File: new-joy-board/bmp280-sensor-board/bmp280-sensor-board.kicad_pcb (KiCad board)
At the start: 2 copper layers, 26.1 x 31.1 mm, 16 parts, among them J1 Conn_01x05, U1 TPS76933, U2 bmp280-board, U3 P82B715, U4 MPU6050_Breakout

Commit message: Continue work on daughter board
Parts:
- removed R3, R4: 0K, Resistor_SMD:R_0805_2012Metric_Pad1.15x1.40mm_HandSolder
- removed REF** (x4): VAL**, new-joy:z_MountPTH_3mm
- added J2: Conn_01x05, Connector_PinHeader_2.54mm:PinHeader_1x05_P2.54mm_Vertical, F.Cu at (123.1, 44.0)
- J1: footprint Connector_PinHeader_2.54mm:PinHeader_1x05_P2.54mm_Horizontal -> Connector_PinHeader_2.54mm:PinHeader_1x05_P2.54mm_Vertical
- R1, R2: moved to F.Cu
- U2: value bmp280-board -> generic-i2c-device; footprint new-joy:bmp280-board-footprint -> new-joy:generic-i2c-device
- U4: value MPU6050_Breakout -> generic-i2c-device; footprint new-joy:MPU6050_Breakout -> new-joy:generic-i2c-device
- moved U4 7.09 mm to (106.8, 49.1), turned to 0 degrees
- moved C2 6.13 mm to (105.4, 47.0), turned to 270 degrees
- moved U1 5.83 mm to (105.7, 53.5), turned to 90 degrees
- moved U2 5.59 mm to (101.7, 49.1), turned to 0 degrees
- moved R2 5.19 mm to (109.9, 44.7), turned to 90 degrees
- moved C3 4.48 mm to (116.1, 47.5)
- moved R1 4.38 mm to (109.9, 50.4), turned to 90 degrees
- moved U3 2.77 mm to (113.7, 48.3)
- moved C1 2.68 mm to (113.7, 51.7), turned to 270 degrees
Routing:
- net +3V3: track 48.5 -> 26.0 mm, vias 0 -> 2
- net /SCL: track 40.0 -> 25.2 mm
- net GND: track 5.26 -> 17.9 mm, vias 2 -> 6
- net /SDABUF: track 8.51 -> 15.1 mm
- net Net-(R3-Pad1): track 5.69 -> 0.00 mm
- net /SCLBUF: track 15.4 -> 9.89 mm
- net +5V: track 22.6 -> 26.9 mm
- net Net-(R4-Pad2): track 3.90 -> 0.00 mm
- net /SDA: track 23.6 -> 21.4 mm
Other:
- board size 26.1 x 31.1 mm -> 30.5 x 14 mm
- net class 3.3V added: clearance 0.2, trace_width 0.4, via_dia 0.8, via_drill 0.4
- net class 5V added: clearance 0.2, trace_width 0.5, via_dia 0.8, via_drill 0.4

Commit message: Prolonged daughter board and added footprint for better soldering
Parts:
- J1, J2: footprint Connector_PinHeader_2.54mm:PinHeader_1x05_P2.54mm_Vertical -> new-joy:Buffered-I2C-Cable-Connector
- moved J1 11.4 mm to (130.1, 44.0)
- moved J2 10.8 mm to (133.9, 44.0)
- moved R1 5.34 mm to (109.9, 45.1), turned to 270 degrees
- moved R2 5.31 mm to (109.8, 50.0), turned to 270 degrees
- moved U3 0.25 mm to (113.6, 48.0), turned to 90 degrees
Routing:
- net +5V: track 26.9 -> 48.4 mm
- net /SCLBUF: track 9.89 -> 23.7 mm
- net /SDABUF: track 15.1 -> 24.8 mm
- net /SCL: track 25.2 -> 21.4 mm
- net +3V3: track 26.0 -> 28.7 mm
- net GND: track 17.9 -> 20.1 mm, vias 6 -> 7
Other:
- board size 30.5 x 14 mm -> 41.3 x 14 mm

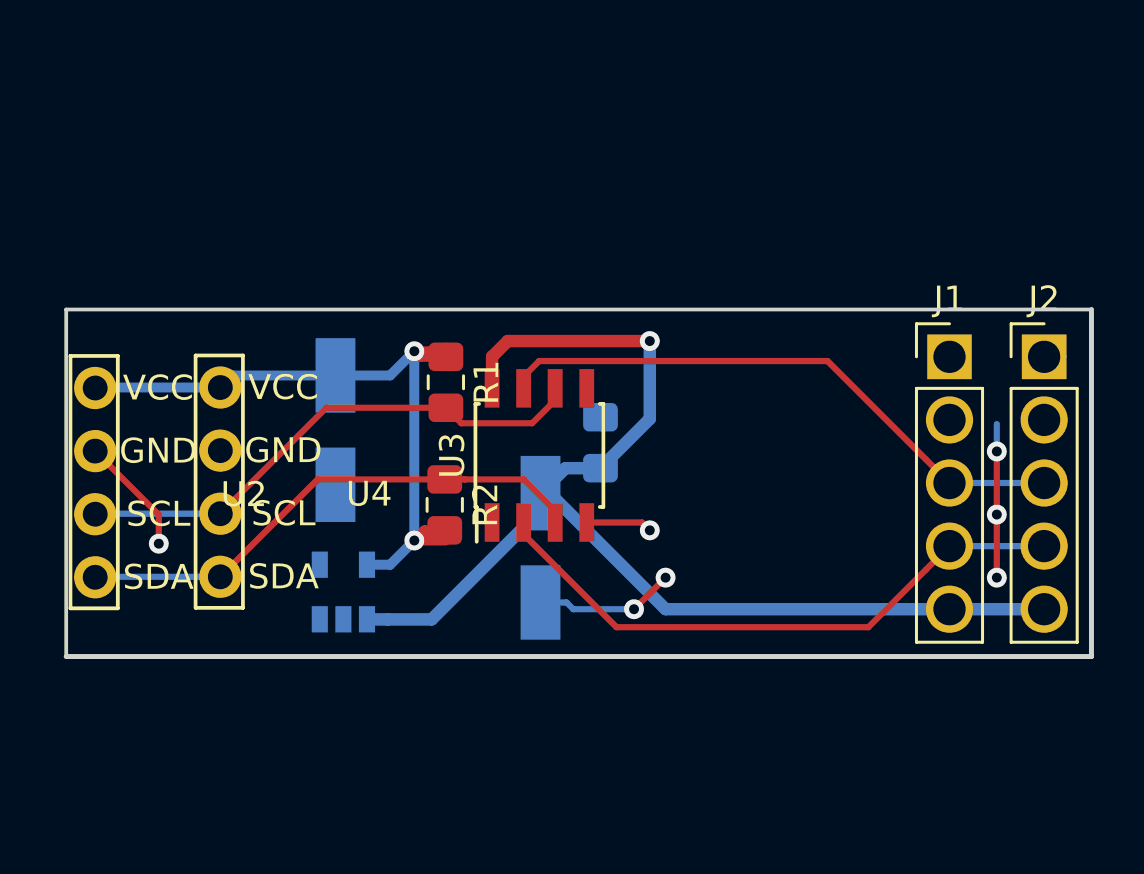
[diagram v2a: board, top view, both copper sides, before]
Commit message: Resized board to conform with multi cb
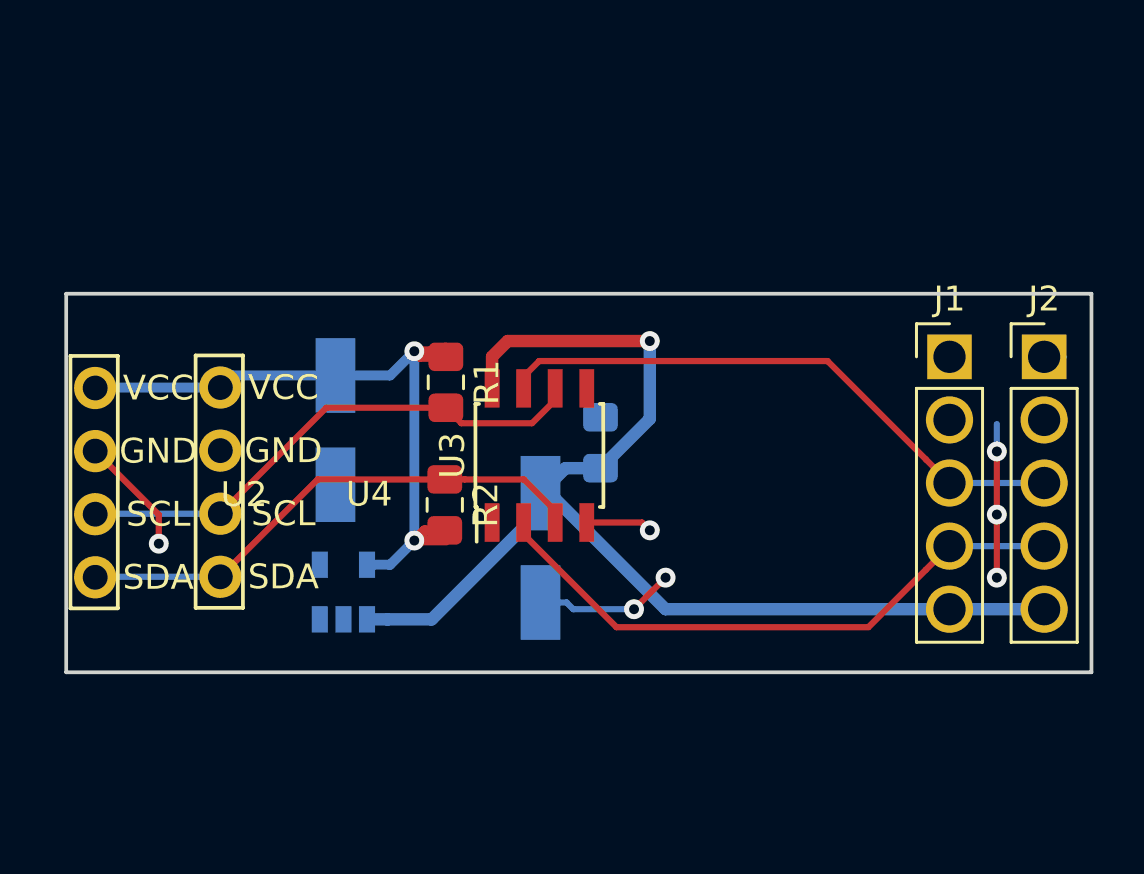
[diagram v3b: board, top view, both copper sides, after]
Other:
- board size 41.3 x 14 mm -> 41.3 x 15.2 mm
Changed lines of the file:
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@@
     (visible_elements FFFFFF7F)
     (pcbplotparams
-      (layerselection 0x010fc_ffffffff)
+      (layerselection 0x010f0_ffffffff)
       (usegerberextensions false)
       (usegerberattributes false)
@@
       (outputformat 1)
       (mirror false)
-      (drillshape 1)
+      (drillshape 0)
       (scaleselection 1)
       (outputdirectory ""))
@@
     )
   )
-  (dimension 13.97 (width 0.3) (layer F.SilkS)
-    (gr_text "13,970 mm" (at 88.66 49.12 90) (layer F.SilkS)
+  (dimension 41.275 (width 0.3) (layer Eco2.User)
+    (gr_text "41,275 mm" (at 115.2075 62.65) (layer Eco2.User)
       (effects (font (size 1.5 1.5) (thickness 0.3)))
     )
-    (feature1 (pts (xy 94.57 42.135) (xy 90.173579 42.135)))
-    (feature2 (pts (xy 94.57 56.105) (xy 90.173579 56.105)))
-    (crossbar (pts (xy 90.76 56.105) (xy 90.76 42.135)))
-    (arrow1a (pts (xy 90.76 42.135) (xy 91.346421 43.261504)))
-    (arrow1b (pts (xy 90.76 42.135) (xy 90.173579 43.261504)))
-    (arrow2a (pts (xy 90.76 56.105) (xy 91.346421 54.978496)))
-    (arrow2b (pts (xy 90.76 56.105) (xy 90.173579 54.978496)))
-  )
-  (gr_line (start 94.57 42.135) (end 135.845 42.135) (layer Edge.Cuts) (width 0.15))
-  (gr_line (start 135.845 56.105) (end 135.845 42.135) (layer Edge.Cuts) (width 0.2))
-  (gr_line (start 94.57 56.105) (end 135.845 56.105) (layer Edge.Cuts) (width 0.2))
-  (dimension 41.275 (width 0.3) (layer F.SilkS)
-    (gr_text "41,275 mm" (at 115.2075 64.555) (layer F.SilkS)
+    (feature1 (pts (xy 135.845 57.375) (xy 135.845 61.136421)))
+    (feature2 (pts (xy 94.57 57.375) (xy 94.57 61.136421)))
+    (crossbar (pts (xy 94.57 60.55) (xy 135.845 60.55)))
+    (arrow1a (pts (xy 135.845 60.55) (xy 134.718496 61.136421)))
+    (arrow1b (pts (xy 135.845 60.55) (xy 134.718496 59.963579)))
+    (arrow2a (pts (xy 94.57 60.55) (xy 95.696504 61.136421)))
+    (arrow2b (pts (xy 94.57 60.55) (xy 95.696504 59.963579)))
+  )
+  (dimension 15.24 (width 0.3) (layer Eco2.User)
+    (gr_text "15,240 mm" (at 88.66 49.12 90) (layer Eco2.User)
       (effects (font (size 1.5 1.5) (thickness 0.3)))
     )
-    (feature1 (pts (xy 135.845 57.375) (xy 135.845 63.041421)))
-    (feature2 (pts (xy 94.57 57.375) (xy 94.57 63.041421)))
-    (crossbar (pts (xy 94.57 62.455) (xy 135.845 62.455)))
-    (arrow1a (pts (xy 135.845 62.455) (xy 134.718496 63.041421)))
-    (arrow1b (pts (xy 135.845 62.455) (xy 134.718496 61.868579)))
-    (arrow2a (pts (xy 94.57 62.455) (xy 95.696504 63.041421)))
-    (arrow2b (pts (xy 94.57 62.455) (xy 95.696504 61.868579)))
-  )
-  (gr_line (start 94.57 56.105) (end 94.57 42.135) (layer Edge.Cuts) (width 0.15))
+    (feature1 (pts (xy 93.935 41.5) (xy 90.173579 41.5)))
+    (feature2 (pts (xy 93.935 56.74) (xy 90.173579 56.74)))
+    (crossbar (pts (xy 90.76 56.74) (xy 90.76 41.5)))
+    (arrow1a (pts (xy 90.76 41.5) (xy 91.346421 42.626504)))
+    (arrow1b (pts (xy 90.76 41.5) (xy 90.173579 42.626504)))
+    (arrow2a (pts (xy 90.76 56.74) (xy 91.346421 55.613496)))
+    (arrow2b (pts (xy 90.76 56.74) (xy 90.173579 55.613496)))
+  )
+  (gr_line (start 135.845 56.74) (end 94.57 56.74) (layer Edge.Cuts) (width 0.15))
+  (gr_line (start 135.845 41.5) (end 135.845 56.74) (layer Edge.Cuts) (width 0.15))
+  (gr_line (start 94.57 41.5) (end 135.845 41.5) (layer Edge.Cuts) (width 0.15))
+  (gr_line (start 94.57 41.5) (end 94.57 56.74) (layer Edge.Cuts) (width 0.15))
   (segment (start 107.505 54.61) (end 106.68 54.61) (width 0.5) (layer B.Cu) (net 1))
   (segment (start 109.285 54.61) (end 107.505 54.61) (width 0.5) (layer B.Cu) (net 1))
@@
     (polygon
       (pts
-        (xy 94.57 42.135) (xy 135.845 42.135) (xy 135.845 56.105) (xy 94.57 56.105)
+        (xy 94.57 41.5) (xy 135.845 41.5) (xy 135.845 56.74) (xy 94.57 56.74)
       )
     )
